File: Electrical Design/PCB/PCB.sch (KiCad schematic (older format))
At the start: 34 parts, among them J1 Conn_02x03_Odd_Even, U1 ADP3338AKCZ-5-R7, U2 BNO080, U3 ADP3338AKCZ-3.3-R7, U4 MS560702BA03-50, U5 SS495A, U6 ATxmega128A4U-AU, Y1 ?

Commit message: a
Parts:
- R1: value R_Small -> 10k
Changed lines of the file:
@@
 P 1650 6950
 F 0 "R1" V 1454 6950 50  0000 C CNN
-F 1 "R_Small" V 1545 6950 50  0000 C CNN
+F 1 "10k" V 1545 6950 50  0000 C CNN
 F 2 "" H 1650 6950 50  0001 C CNN
 F 3 "~" H 1650 6950 50  0001 C CNN
@@
 Wire Notes Line
 	5100 7550 5100 6500
-Wire Notes Line
-	650  6500 650  7050
-Wire Notes Line
-	650  7050 1300 7050
-Wire Notes Line
-	1300 7050 1300 7550
-Wire Notes Line
-	1300 7550 1450 7550
-Wire Notes Line
-	1450 7550 1450 7050
-Wire Notes Line
-	1450 7050 1900 7050
-Wire Notes Line
-	1900 7050 1900 7250
-Wire Notes Line
-	1900 7250 2100 7250
-Wire Notes Line
-	2100 7250 2100 6800
-Wire Notes Line
-	2100 6800 1800 6800
-Wire Notes Line
-	1800 6800 1800 6650
-Wire Notes Line
-	1800 6650 1700 6650
-Wire Notes Line
-	1700 6650 1700 6500
-Wire Notes Line
-	1700 6500 650  6500
 $EndSCHEMATC

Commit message: update
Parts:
- added MOD?: XBP9B-DMWT-002, digikey-footprints:XBEE_PRO-20_THT, symbol dk_RF-Transceiver-Modules:XBP9B-DMWT-002
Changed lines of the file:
@@
 Wire Notes Line
 	5100 7550 5100 6500
+$Comp
+L dk_RF-Transceiver-Modules:XBP9B-DMWT-002 MOD?
+U 1 1 5C555561
+P 4900 2000
+F 0 "MOD?" H 4950 1706 60  0000 C CNN
+F 1 "XBP9B-DMWT-002" H 4950 1600 60  0000 C CNN
+F 2 "digikey-footprints:XBEE_PRO-20_THT" H 5100 2200 60  0001 L CNN
+F 3 "https://www.digi.com/resources/documentation/digidocs/pdfs/90002173.pdf" H 5100 2300 60  0001 L CNN
+F 4 "602-1301-ND" H 5100 2400 60  0001 L CNN "Digi-Key_PN"
+F 5 "XBP9B-DMWT-002" H 5100 2500 60  0001 L CNN "MPN"
+F 6 "RF/IF and RFID" H 5100 2600 60  0001 L CNN "Category"
+F 7 "RF Transceiver Modules" H 5100 2700 60  0001 L CNN "Family"
+F 8 "https://www.digi.com/resources/documentation/digidocs/pdfs/90002173.pdf" H 5100 2800 60  0001 L CNN "DK_Datasheet_Link"
+F 9 "/product-detail/en/digi-international/XBP9B-DMWT-002/602-1301-ND/3594159" H 5100 2900 60  0001 L CNN "DK_Detail_Page"
+F 10 "RF TXRX MODULE ISM<1GHZ WIRE ANT" H 5100 3000 60  0001 L CNN "Description"
+F 11 "Digi International" H 5100 3100 60  0001 L CNN "Manufacturer"
+F 12 "Active" H 5100 3200 60  0001 L CNN "Status"
+	1    4900 2000
+	1    0    0    -1
+$EndComp
 $EndSCHEMATC

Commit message: Datalogger, GPS, Radio
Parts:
- added C?: 1uF, symbol Device:C_Small
- added C?: 47pF, symbol Device:C_Small
- added U?: Adafruit_746, symbol Skyfire_Custom_Components:Adafruit_746
- added U?: Openlog, symbol Skyfire_Custom_Components:Openlog
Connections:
- net labels added: GPS_MISO, GPS_MOSI, GPS_RX, GPS_TX, OpenLog_MISO, OpenLog_MOSI, PA5-Hall_Effect, PA5-Hall_effect, ~SS_5607, ~SS_BNO080, ~SS_XBEE
- net labels removed: SS_5607, SS_BNO080, UNASSIGNED
- wire segments 114 -> 128
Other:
- note added: "XBEE"
- note removed: "RX"
- note removed: "TX\n"
- moved on the sheet: MOD?

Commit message: Schemat_Done?
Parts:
- added D?: 3V3 Status, symbol Device:LED
- added D?: 5V Status, symbol Device:LED
- added D?: 6V Status, symbol Device:LED
- added D?: Power Status, symbol Device:LED
- added M?: Release_Servo, symbol Motor:Motor_Servo
- added M?: Camera_Servo, symbol Motor:Motor_Servo
- added Q?: LED_MOS, digikey-footprints:SOT-23-3, symbol dk_Transistors-FETs-MOSFETs-Single:2N7002K-T1-E3
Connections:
- net labels added: Camera_Servo, LED_MOS, OpenLog_GRN, Release_Servo
- net labels removed: -3V3, -5V
- wire segments 128 -> 153

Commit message: Forget the Fets
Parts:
- added Q?: CAMERA_MOS, digikey-footprints:SOT-23-3, symbol dk_Transistors-FETs-MOSFETs-Single:2N7002K-T1-E3
- added Q?: RELEASE_MOS, digikey-footprints:SOT-23-3, symbol dk_Transistors-FETs-MOSFETs-Single:2N7002K-T1-E3
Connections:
- net GND: now also Q?.2 (S), Q?.2 (S); no longer M?.3 (-), M?.3 (-)
- net RELEASE_MOS: now reaches U6.26 (PD6)
- net RELEASE_MOS: now also Q?.1 (G)
- net CAMERA_MOS: now reaches U6.27 (PD7)
- net CAMERA_MOS: now also Q?.1 (G)
- new net: M?.3 (-), Q?.3 (D) (x2)
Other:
- moved on the sheet: M?
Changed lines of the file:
@@
 	1    0    0    -1
 $EndComp
-Text Notes 8800 5400 0    50   ~ 0
+Text Notes 8850 5350 0    50   ~ 0
 TC
-Text Notes 8800 5500 0    50   ~ 0
+Text Notes 8850 5450 0    50   ~ 0
 TC
 $Comp
@@
 L Motor:Motor_Servo M?
 U 1 1 5C6F6AC9
-P 8900 1000
-F 0 "M?" H 9232 1065 50  0000 L CNN
-F 1 "Release_Servo" H 9232 974 50  0000 L CNN
-F 2 "" H 8900 810 50  0001 C CNN
-F 3 "http://forums.parallax.com/uploads/attachments/46831/74481.png" H 8900 810 50  0001 C CNN
-	1    8900 1000
+P 8800 1050
+F 0 "M?" H 9132 1115 50  0000 L CNN
+F 1 "Release_Servo" H 9132 1024 50  0000 L CNN
+F 2 "" H 8800 860 50  0001 C CNN
+F 3 "http://forums.parallax.com/uploads/attachments/46831/74481.png" H 8800 860 50  0001 C CNN
+	1    8800 1050
 	1    0    0    -1
 $EndComp
@@
 L Motor:Motor_Servo M?
 U 1 1 5C6F7803
-P 8900 1750
-F 0 "M?" H 9231 1815 50  0000 L CNN
-F 1 "Camera_Servo" H 9231 1724 50  0000 L CNN
-F 2 "" H 8900 1560 50  0001 C CNN
-F 3 "http://forums.parallax.com/uploads/attachments/46831/74481.png" H 8900 1560 50  0001 C CNN
-	1    8900 1750
+P 8800 2100
+F 0 "M?" H 9131 2165 50  0000 L CNN
+F 1 "Camera_Servo" H 9131 2074 50  0000 L CNN
+F 2 "" H 8800 1910 50  0001 C CNN
+F 3 "http://forums.parallax.com/uploads/attachments/46831/74481.png" H 8800 1910 50  0001 C CNN
+	1    8800 2100
 	1    0    0    -1
 $EndComp
@@
 L power:+6V #PWR?
 U 1 1 5C6F83F2
-P 8450 1000
-F 0 "#PWR?" H 8450 850 50  0001 C CNN
-F 1 "+6V" V 8465 1128 50  0000 L CNN
-F 2 "" H 8450 1000 50  0001 C CNN
-F 3 "" H 8450 1000 50  0001 C CNN
-	1    8450 1000
+P 8350 1050
+F 0 "#PWR?" H 8350 900 50  0001 C CNN
+F 1 "+6V" V 8365 1178 50  0000 L CNN
+F 2 "" H 8350 1050 50  0001 C CNN
+F 3 "" H 8350 1050 50  0001 C CNN
+	1    8350 1050
 	0    -1   -1   0
 $EndComp
@@
 L power:GND #PWR?
 U 1 1 5C6F875E
-P 8450 1150
-F 0 "#PWR?" H 8450 900 50  0001 C CNN
-F 1 "GND" H 8455 977 50  0000 C CNN
-F 2 "" H 8450 1150 50  0001 C CNN
-F 3 "" H 8450 1150 50  0001 C CNN
-	1    8450 1150
+P 10600 1050
+F 0 "#PWR?" H 10600 800 50  0001 C CNN
+F 1 "GND" H 10750 1000 50  0000 C CNN
+F 2 "" H 10600 1050 50  0001 C CNN
+F 3 "" H 10600 1050 50  0001 C CNN
+	1    10600 1050
 	1    0    0    -1
 $EndComp
@@
 L power:GND #PWR?
 U 1 1 5C6F8A5A
-P 8450 1900
-F 0 "#PWR?" H 8450 1650 50  0001 C CNN
-F 1 "GND" H 8455 1727 50  0000 C CNN
-F 2 "" H 8450 1900 50  0001 C CNN
-F 3 "" H 8450 1900 50  0001 C CNN
-	1    8450 1900
+P 10600 2150
+F 0 "#PWR?" H 10600 1900 50  0001 C CNN
+F 1 "GND" H 10750 2100 50  0000 C CNN
+F 2 "" H 10600 2150 50  0001 C CNN
+F 3 "" H 10600 2150 50  0001 C CNN
+	1    10600 2150
 	1    0    0    -1
 $EndComp
@@
 L power:+6V #PWR?
 U 1 1 5C6F8FC9
-P 8450 1750
-F 0 "#PWR?" H 8450 1600 50  0001 C CNN
-F 1 "+6V" V 8465 1878 50  0000 L CNN
-F 2 "" H 8450 1750 50  0001 C CNN
-F 3 "" H 8450 1750 50  0001 C CNN
-	1    8450 1750
+P 8350 2100
+F 0 "#PWR?" H 8350 1950 50  0001 C CNN
+F 1 "+6V" V 8365 2228 50  0000 L CNN
+F 2 "" H 8350 2100 50  0001 C CNN
+F 3 "" H 8350 2100 50  0001 C CNN
+	1    8350 2100
 	0    -1   -1   0
 $EndComp
 Wire Wire Line
-	8450 1750 8600 1750
-Wire Wire Line
-	8450 1900 8450 1850
-Wire Wire Line
-	8450 1850 8600 1850
-Wire Wire Line
-	8450 1150 8450 1100
-Wire Wire Line
-	8450 1100 8600 1100
-Wire Wire Line
-	8450 1000 8600 1000
+	8350 2100 8500 2100
+Wire Wire Line
+	8350 1050 8500 1050
 Text Label 8950 4550 2    50   ~ 0
 Release_Servo
 Text Label 8950 4450 2    50   ~ 0
 Camera_Servo
-Text Label 8600 1650 2    50   ~ 0
+Text Label 8500 2000 2    50   ~ 0
 Camera_Servo
-Text Label 8600 900  2    50   ~ 0
+Text Label 8500 950  2    50   ~ 0
 Release_Servo
+$Comp
+L dk_Transistors-FETs-MOSFETs-Single:2N7002K-T1-E3 Q?
+U 1 1 5C72FE6D
+P 10250 1000
+F 0 "Q?" H 10358 947 60  0000 L CNN
+F 1 "RELEASE_MOS" V 10358 1053 60  0000 L CNN
+F 2 "digikey-footprints:SOT-23-3" H 10450 1200 60  0001 L CNN
+F 3 "http://www.vishay.com/docs/71333/2n7002k.pdf" H 10450 1300 60  0001 L CNN
+F 4 "2N7002K-T1-E3CT-ND" H 10450 1400 60  0001 L CNN "Digi-Key_PN"
+F 5 "2N7002K-T1-E3" H 10450 1500 60  0001 L CNN "MPN"
+F 6 "Discrete Semiconductor Products" H 10450 1600 60  0001 L CNN "Category"
+F 7 "Transistors - FETs, MOSFETs - Single" H 10450 1700 60  0001 L CNN "Family"
+F 8 "http://www.vishay.com/docs/71333/2n7002k.pdf" H 10450 1800 60  0001 L CNN "DK_Datasheet_Link"
+F 9 "/product-detail/en/vishay-siliconix/2N7002K-T1-E3/2N7002K-T1-E3CT-ND/1656760" H 10450 1900 60  0001 L CNN "DK_Detail_Page"
+F 10 "MOSFET N-CH 60V 300MA SOT-23" H 10450 2000 60  0001 L CNN "Description"
+F 11 "Vishay Siliconix" H 10450 2100 60  0001 L CNN "Manufacturer"
+F 12 "Active" H 10450 2200 60  0001 L CNN "Status"
+	1    10250 1000
+	0    -1   -1   0
+$EndComp
+Wire Wire Line
+	10450 1000 10600 1000
+Wire Wire Line
+	10600 1000 10600 1050
+Wire Wire Line
+	10450 2100 10600 2100
+Wire Wire Line
+	10600 2100 10600 2150
+Wire Wire Line
+	8500 1150 8500 1250
+Wire Wire Line
+	8500 1250 10050 1250
+Wire Wire Line
+	10050 1250 10050 1000
+Wire Wire Line
+	8500 2200 8500 2300
+Wire Wire Line
+	10050 2300 10050 2100
+Wire Wire Line
+	8500 2300 10050 2300
+$Comp
+L dk_Transistors-FETs-MOSFETs-Single:2N7002K-T1-E3 Q?
+U 1 1 5C72F9D1
+P 10250 2100
+F 0 "Q?" H 10358 2047 60  0000 L CNN
+F 1 "CAMERA_MOS" V 10358 2153 60  0000 L CNN
+F 2 "digikey-footprints:SOT-23-3" H 10450 2300 60  0001 L CNN
+F 3 "http://www.vishay.com/docs/71333/2n7002k.pdf" H 10450 2400 60  0001 L CNN
+F 4 "2N7002K-T1-E3CT-ND" H 10450 2500 60  0001 L CNN "Digi-Key_PN"
+F 5 "2N7002K-T1-E3" H 10450 2600 60  0001 L CNN "MPN"
+F 6 "Discrete Semiconductor Products" H 10450 2700 60  0001 L CNN "Category"
+F 7 "Transistors - FETs, MOSFETs - Single" H 10450 2800 60  0001 L CNN "Family"
+F 8 "http://www.vishay.com/docs/71333/2n7002k.pdf" H 10450 2900 60  0001 L CNN "DK_Datasheet_Link"
+F 9 "/product-detail/en/vishay-siliconix/2N7002K-T1-E3/2N7002K-T1-E3CT-ND/1656760" H 10450 3000 60  0001 L CNN "DK_Detail_Page"
+F 10 "MOSFET N-CH 60V 300MA SOT-23" H 10450 3100 60  0001 L CNN "Description"
+F 11 "Vishay Siliconix" H 10450 3200 60  0001 L CNN "Manufacturer"
+F 12 "Active" H 10450 3300 60  0001 L CNN "Status"
+	1    10250 2100
+	0    -1   -1   0
+$EndComp
+Text Label 10350 2400 3    50   ~ 0
+CAMERA_MOS
+Text Label 10350 1300 3    50   ~ 0
+RELEASE_MOS
+Text Label 8950 5650 2    50   ~ 0
+CAMERA_MOS
+Text Label 8950 5550 2    50   ~ 0
+RELEASE_MOS
 $EndSCHEMATC

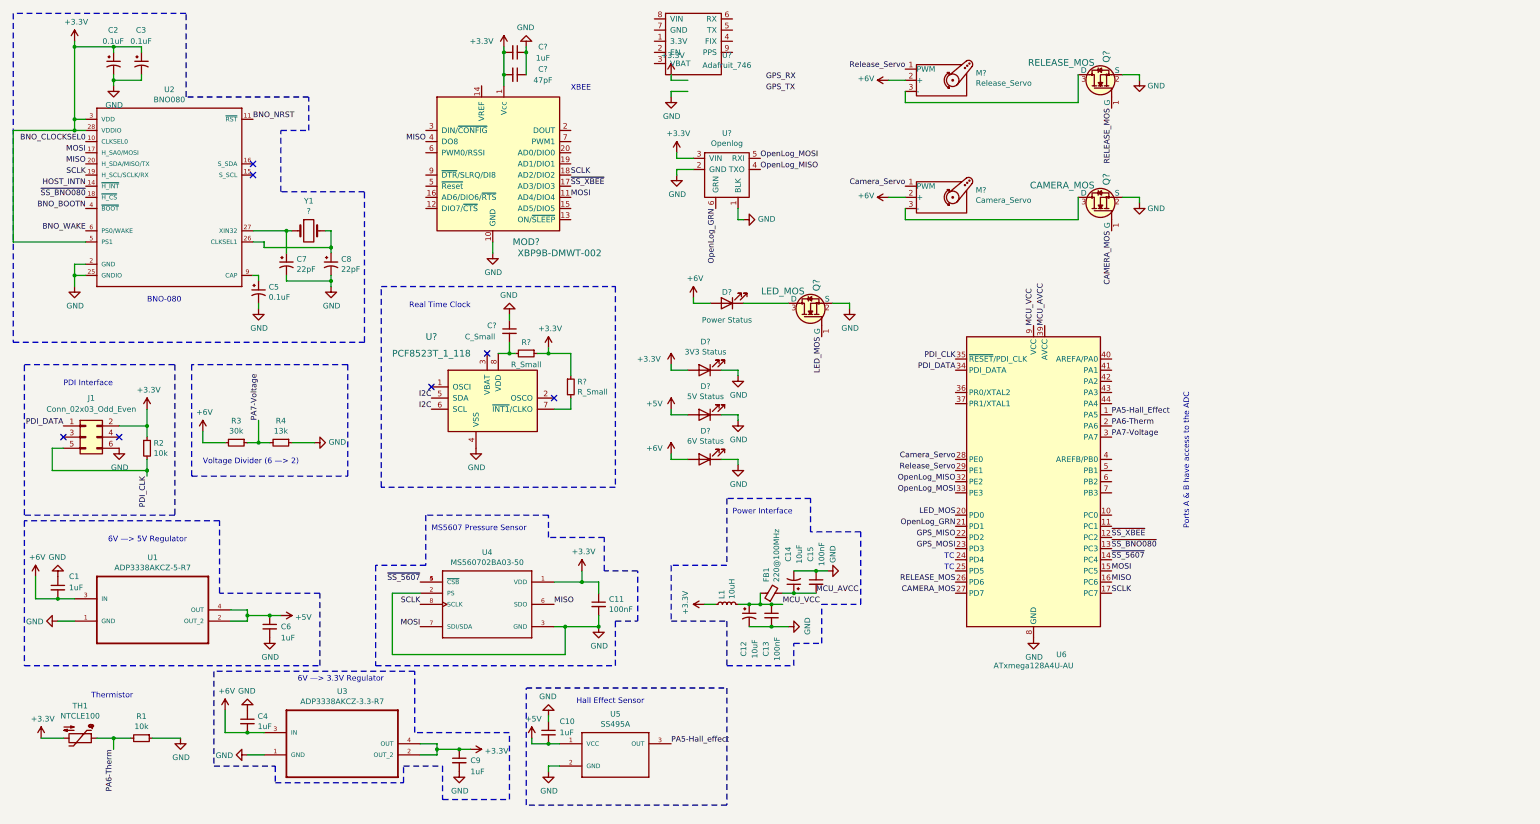
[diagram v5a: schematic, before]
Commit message: Assign footprints
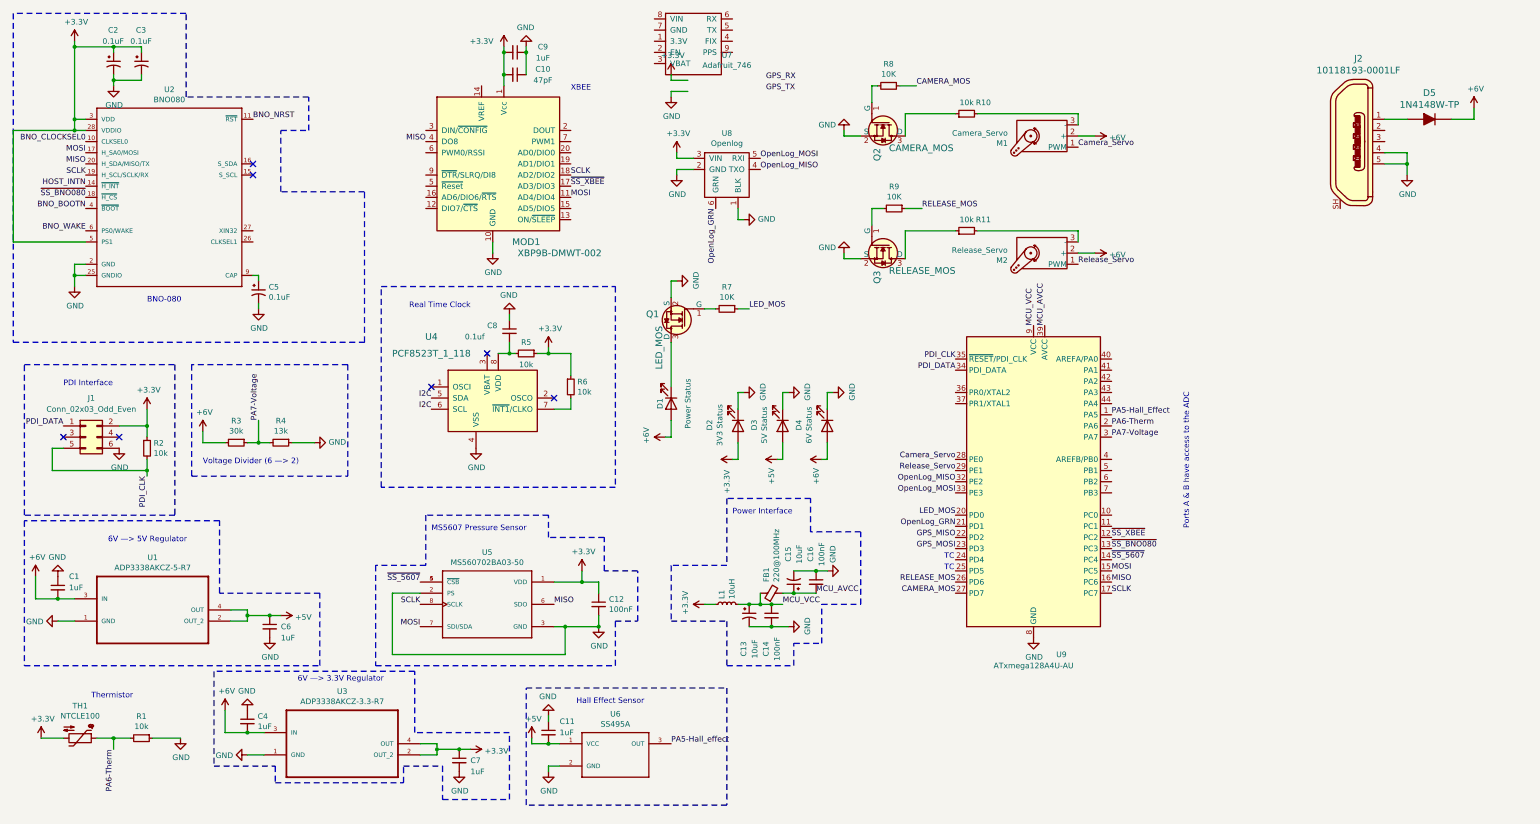
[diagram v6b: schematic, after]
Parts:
- removed C7, C8: 22pF, symbol Device:CP1_Small
- removed Y1: ?, symbol Device:Crystal
- added D5: 1N4148W-TP, digikey-footprints:SOD-123, symbol dk_Diodes-Rectifiers-Single:1N4148W-TP
- added J2: 10118193-0001LF, digikey-footprints:USB_Micro_B_Female_10118193-0001LF, symbol dk_USB-DVI-HDMI-Connectors:10118193-0001LF
- added R10, R11: 10k, Resistor_SMD:R_0805_2012Metric, symbol Device:R_Small
- added R7, R8, R9: 10K, Resistor_SMD:R_0805_2012Metric, symbol Device:R_Small
- C1, C4, C6: footprint (none) -> Capacitor_SMD:C_0805_2012Metric_Pad1.15x1.40mm_HandSolder
- C10, C9: renamed from C?; footprint (none) -> Capacitor_SMD:C_0805_2012Metric_Pad1.15x1.40mm_HandSolder
- C11: renamed from C10; footprint (none) -> Capacitor_SMD:C_0805_2012Metric_Pad1.15x1.40mm_HandSolder
- C12: renamed from C11; footprint (none) -> Capacitor_SMD:C_0805_2012Metric_Pad1.15x1.40mm_HandSolder
- C14: renamed from C13; footprint (none) -> Capacitor_SMD:C_0805_2012Metric_Pad1.15x1.40mm_HandSolder
- C16: renamed from C15; footprint (none) -> Capacitor_SMD:C_0805_2012Metric_Pad1.15x1.40mm_HandSolder
- C7: renamed from C9; footprint (none) -> Capacitor_SMD:C_0805_2012Metric_Pad1.15x1.40mm_HandSolder
- C8: renamed from C?; value C_Small -> 0.1uf; footprint (none) -> Capacitor_SMD:C_0805_2012Metric_Pad1.15x1.40mm_HandSolder
- D1, D2, D3, D4: renamed from D?; footprint (none) -> LED_SMD:LED_0603_1608Metric_Pad1.05x0.95mm_HandSolder
- FB1, L1: footprint (none) -> Inductor_SMD:L_0805_2012Metric_Pad1.15x1.40mm_HandSolder
- R1, R2, R3, R4: footprint (none) -> Resistor_SMD:R_0805_2012Metric
- R5, R6: renamed from R?; value R_Small -> 10k; footprint (none) -> Resistor_SMD:R_0805_2012Metric
- TH1: footprint (none) -> Resistor_THT:R_Axial_Power_L48.0mm_W12.5mm_P55.88mm
- U1, U3: footprint SOT230P700X180-4N -> (none)
- U2: footprint LGA-28 -> (none)
- U5: renamed from U4; footprint SON125P300X500X100-8N -> (none)
- U6: renamed from U5; footprint SIP3-UA -> (none)
- gave numbers to parts that had none: 9
- renumbered C12 to C13, C14 to C15, U6 to U9
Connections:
- net +6V: now also D5.K
- net CAMERA_MOS: now also R8.1; no longer Q2.1 (G)
- net GND: now also J2.4, J2.5
- net LED_MOS: now also R7.1; no longer Q1.1 (G)
- net RELEASE_MOS: now also R9.1; no longer Q3.1 (G)
- net at M2.3 (-): now also R11.2; no longer Q3.3 (D)
- net at M1.3 (-): now also R10.2; no longer Q2.3 (D)
- new net: Q1.1 (G), R7.2
- new net: Q2.1 (G), R8.2
- new net: Q2.3 (D), R10.1
- new net: Q3.1 (G), R9.2
- new net: Q3.3 (D), R11.1
- new net: D5.A, J2.1
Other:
- moved on the sheet: D1, D2, D3, D4, M1, M2, Q1, Q2, Q3
